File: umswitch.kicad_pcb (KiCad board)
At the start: 2 copper layers, 60 x 48 mm, 44 parts, among them J1 Conn_ARM_SWD_TagConnect_TC203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, J2 Micro_SD_Card_Det2, J3 USB_A, J4 Conn_01x16_MountingPin, J5 Conn_01x07, J6 Conn_01x07, SW1 SW_Push, SW2 SW_Push, SW3 SW_Push, U1 LPC5526JBD64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

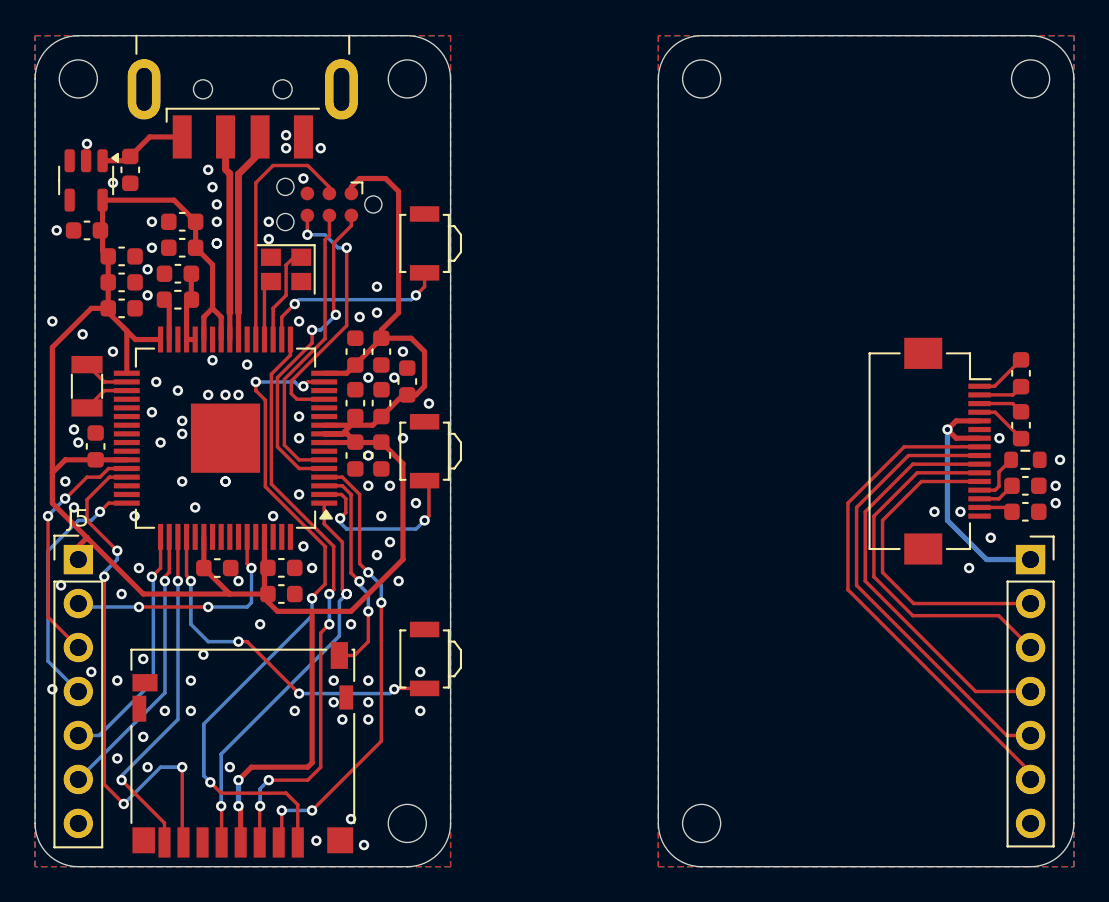
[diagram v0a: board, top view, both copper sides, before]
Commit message: fix some drc issues
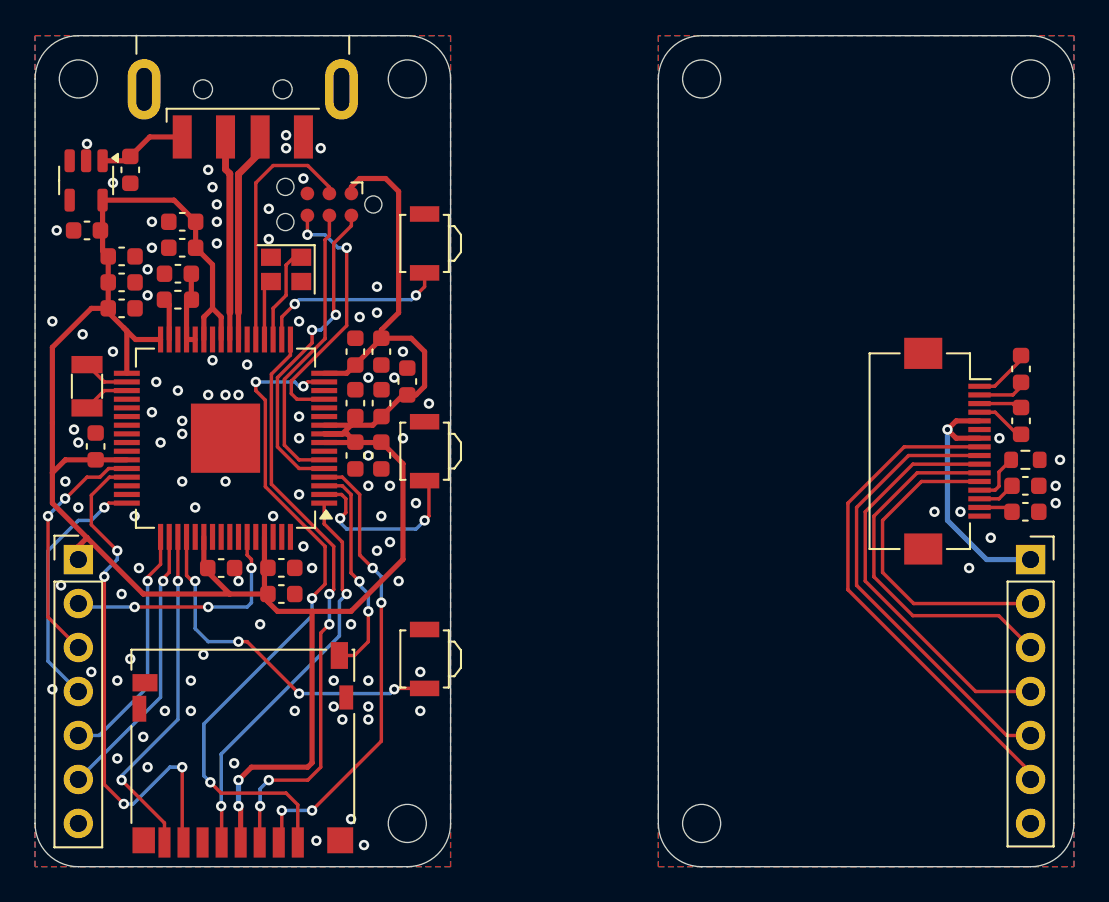
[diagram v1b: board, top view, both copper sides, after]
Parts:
- moved C20 0.25 mm to (167.9, 91.2)
- moved C21 0.25 mm to (167.9, 94.2)
- moved C6 0.22 mm to (121.8, 102.8)
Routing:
- net GND: vias 95 -> 93
- net /SD_CLK: vias 3 -> 2
